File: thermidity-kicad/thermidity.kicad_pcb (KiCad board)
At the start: 2 copper layers, 21 parts, among them J1 Battery, J2 Display, J3 ISP, U1 ATmega328P-A, U2 MCP1501-30xSN, U3 TMP36GT9, U4 HIH-5030-001, Y1 32.768kHz Watch Crystal 10pF 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

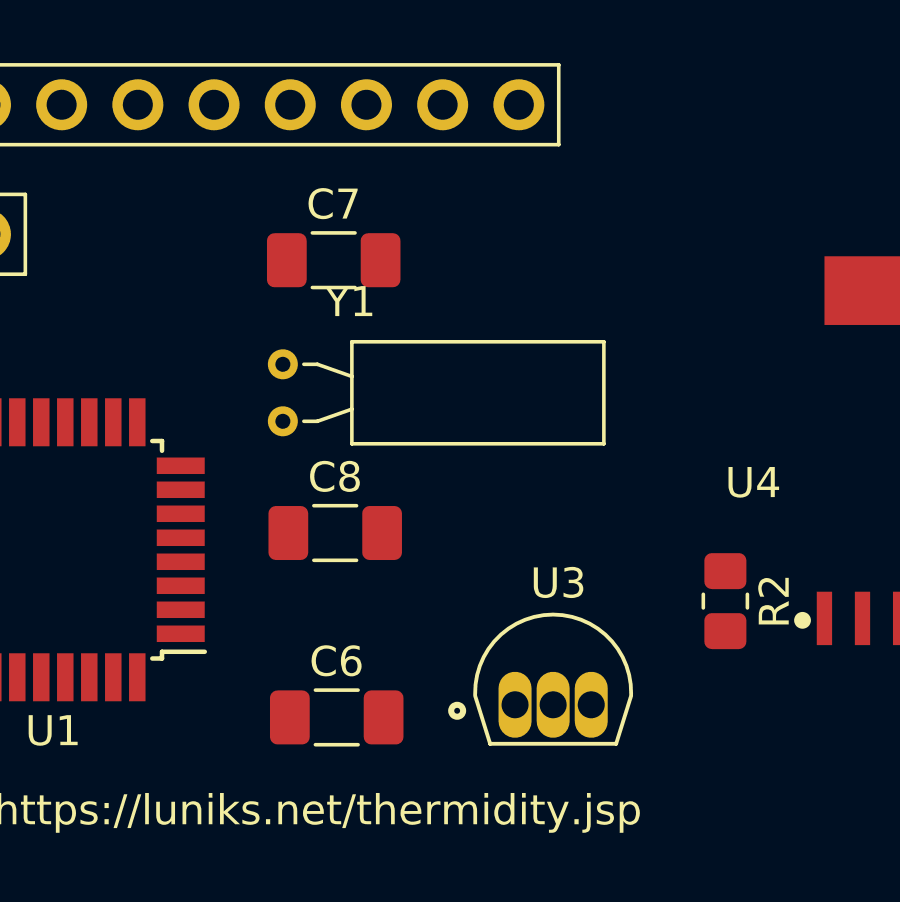
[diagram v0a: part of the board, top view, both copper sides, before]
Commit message: update README, schematic + PCB (remove crystal)
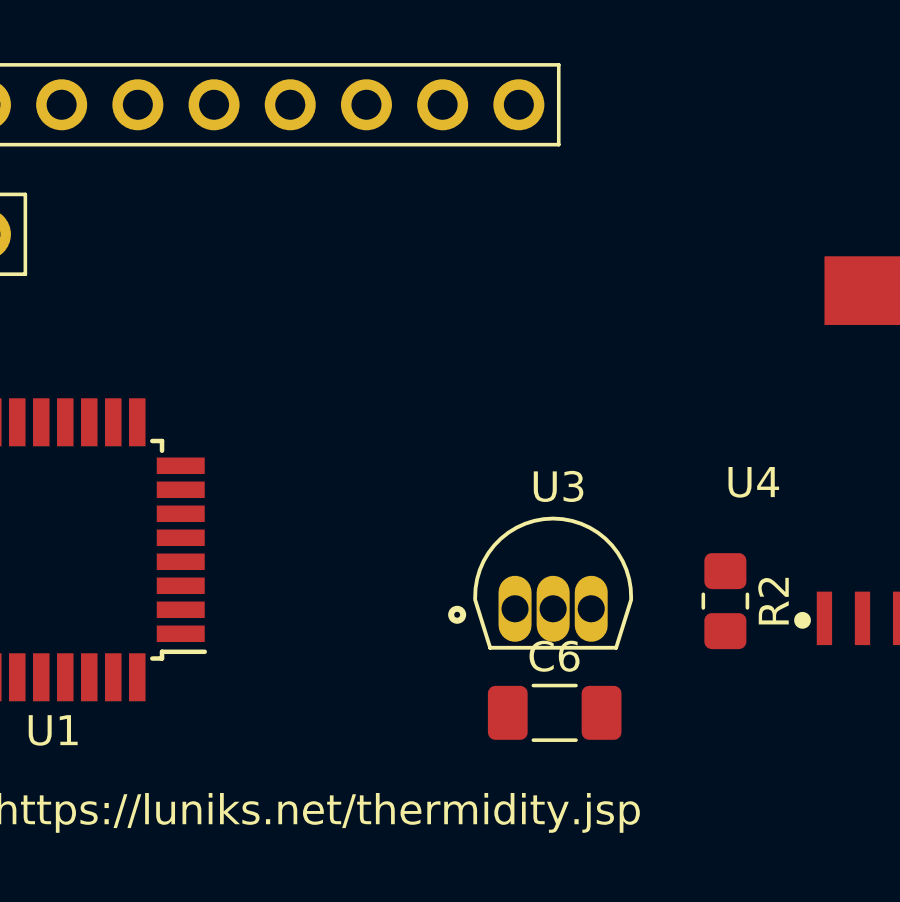
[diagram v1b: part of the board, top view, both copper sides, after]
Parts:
- removed C7, C8: 18pF, Capacitor_SMD:C_1206_3216Metric_Pad1.33x1.80mm_HandSolder
- removed Y1: 32.768kHz Watch Crystal 10pF 35kOhm, Crystal:Crystal_C38-LF_D3.0mm_L8.0mm_Horizontal
- moved C6 7.27 mm to (158.1, 81.0)
- moved U3 3.20 mm to (158.1, 76.7)
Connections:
- U1 pad 7: Net-(C8-Pad1) -> unconnected-(U1-Pad7)
- U1 pad 8: Net-(C7-Pad1) -> unconnected-(U1-Pad8)

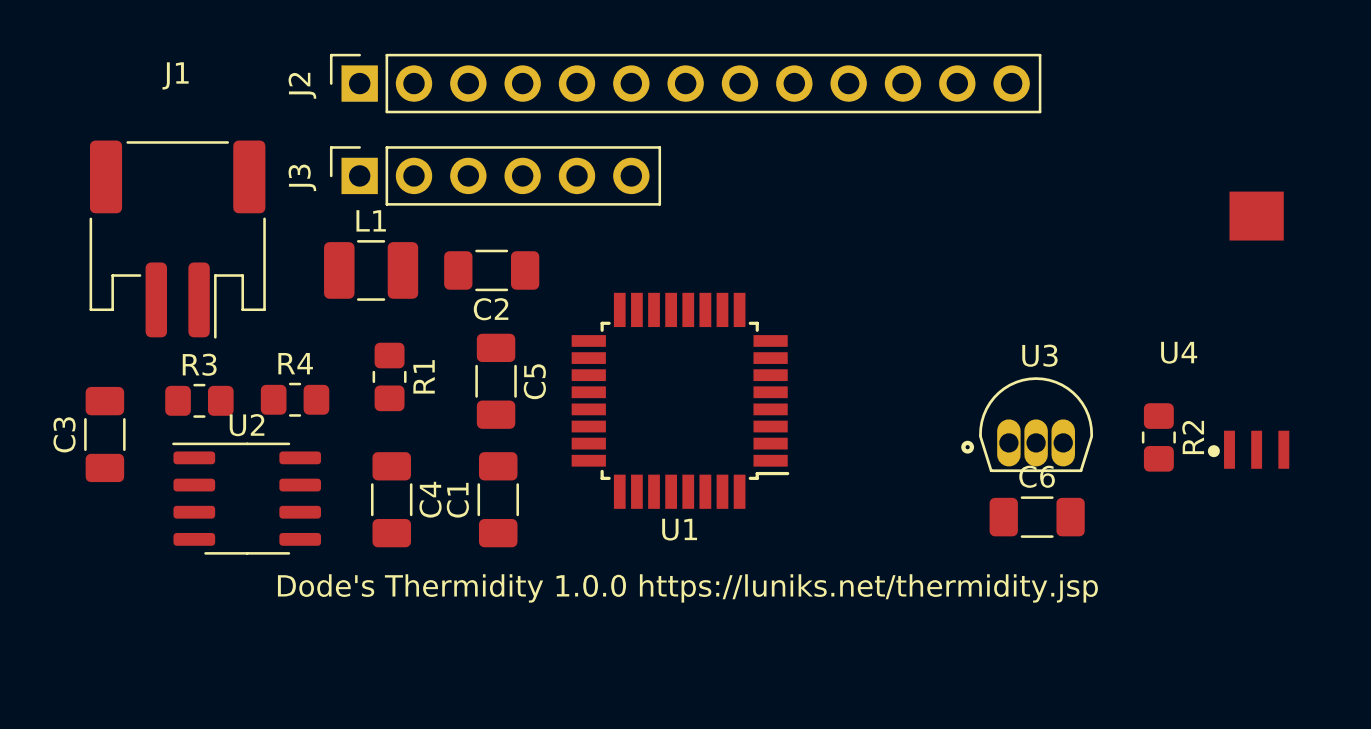
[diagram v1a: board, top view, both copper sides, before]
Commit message: improve PCB, add comments
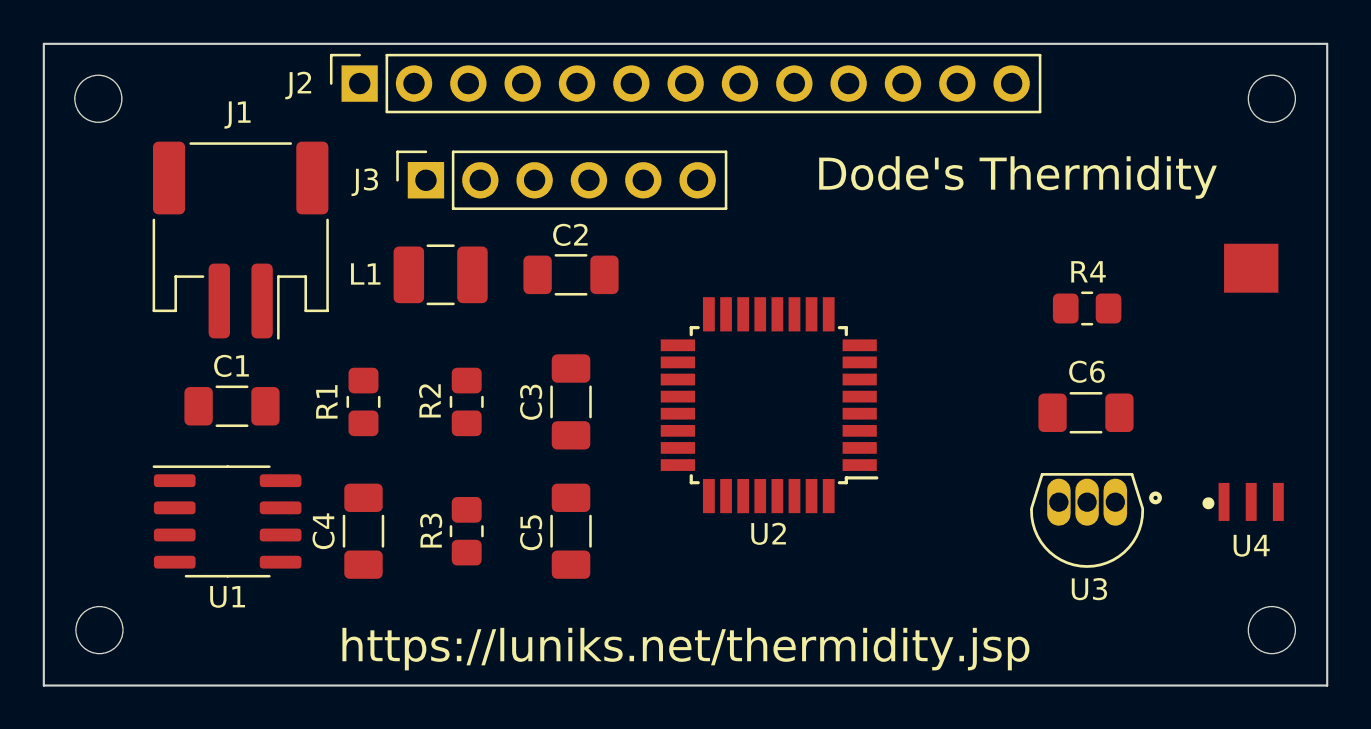
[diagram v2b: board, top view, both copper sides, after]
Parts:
- added H1: M2, MountingHole:MountingHole_2.2mm_M2, F.Cu at (114.2, 61.5)
- added H2: M2, MountingHole:MountingHole_2.2mm_M2, F.Cu at (169.1, 61.5)
- added H3: M2, MountingHole:MountingHole_2.2mm_M2, F.Cu at (114.3, 86.3)
- added H4: M2, MountingHole:MountingHole_2.2mm_M2, F.Cu at (169.1, 86.3)
- U1: renamed from U2; value MCP1501-30xSN -> MCP1501-30
- U2: renamed from U1; value ATmega328P-A -> ATmega328P
- U3: value TMP36GT9 -> TMP36
- U4: value HIH-5030-001 -> HIH-5030
- moved R2 12.5 mm to (131.5, 75.6), turned to -90 degrees
- moved R3 10.1 mm to (131.5, 81.7), turned to -90 degrees
- moved R4 6.90 mm to (160.5, 71.3), turned to 180 degrees
- moved C1 6.09 mm to (120.5, 75.8), turned to 0 degrees
- moved C6 5.39 mm to (160.4, 76.1), turned to 180 degrees
- moved U3 5.16 mm to (160.5, 81.2), turned to 180 degrees
- moved U2 4.17 mm to (145.6, 75.8)
- moved C2 3.71 mm to (136.3, 69.7), turned to 0 degrees
- moved C5 3.71 mm to (136.3, 81.7)
- moved C3 3.64 mm to (136.3, 75.6), turned to 90 degrees
- moved L1 3.26 mm to (130.3, 69.7)
- moved J3 3.11 mm to (129.6, 65.3)
- moved J1 2.95 mm to (120.9, 68.1)
- moved U4 2.45 mm to (168.1, 75.0)
- moved C4 1.98 mm to (126.6, 81.7)
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- renumbered C3 to C1, C5 to C3, C1 to C5, R3 to R2, R4 to R3, R2 to R4
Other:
- board outline added: 60 x 30 mm
- board text added: "Dode's Thermidity"
- board text added: "https://luniks.net/thermidity.jsp"
- board text removed: "Dode's Thermidity 1.0.0 https://luniks.net/thermidity.jsp"

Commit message: improve PCB, add comments
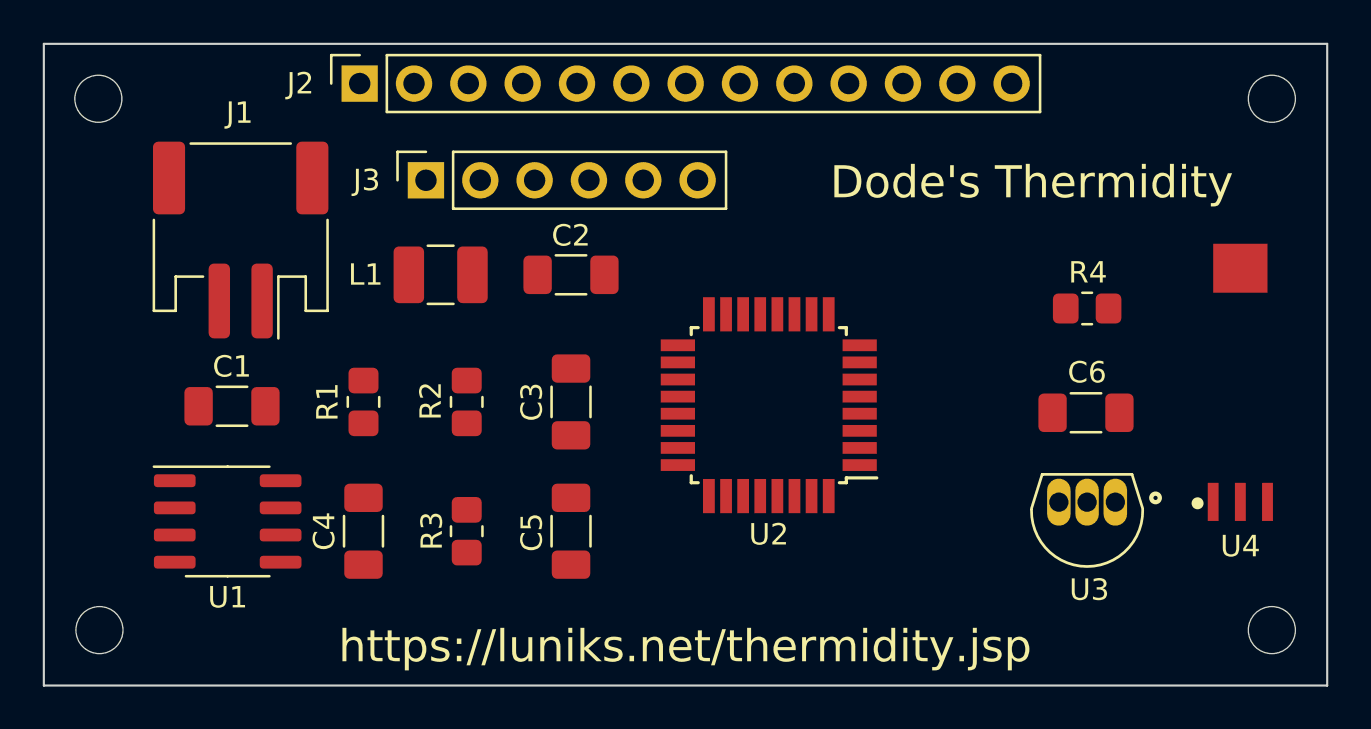
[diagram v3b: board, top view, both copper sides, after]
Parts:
- R1: value 50Ohm -> 50
- moved U4 0.51 mm to (167.6, 75.0)
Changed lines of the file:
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@@
   )
   (footprint "HIH-5030-001:HONEYWELL_HIH-5030-001" (layer "F.Cu")
-    (at 168.148 74.9808)
+    (at 167.64 74.9808)
     (property "AVAILABILITY" "Good")
     (property "MF" "Honeywell")
@@
       (effects (font (size 1 1) (thickness 0.15)))
     )
-    (fp_text value "50Ohm" (at 0 -1.778 90) (layer "F.Fab")
+    (fp_text value "50" (at 0 -1.778 90) (layer "F.Fab")
       (effects (font (size 1 1) (thickness 0.15)))
     )
@@
   (gr_rect (start 111.7 58.9) (end 171.7 88.9) (layer "Edge.Cuts") (width 0.1) (fill none))
   (gr_rect (start 111.7 58.9) (end 171.7 88.9) (layer "F.CrtYd") (width 0.05) (fill none))
-  (gr_text "Dode's Thermidity" (at 157.1752 65.024) (layer "F.SilkS")
+  (gr_text "Dode's Thermidity" (at 157.8864 65.3796) (layer "F.SilkS")
     (effects (font (size 1.5 1.5) (thickness 0.15)))
   )

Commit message: improve PCB
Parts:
- moved C5 25.9 mm to (136.0, 84.8), turned to -90 degrees
- moved U3 19.5 mm to (141.3, 84.8), turned to -90 degrees
- moved C6 18.8 mm to (153.4, 73.9)
- moved R4 18.2 mm to (148.3, 84.8)
- moved U4 13.5 mm to (158.4, 84.8), turned to -90 degrees
- moved C1 9.95 mm to (130.2, 73.7), turned to 180 degrees
- moved R2 7.02 mm to (137.0, 77.4), turned to 180 degrees
- moved R3 6.96 mm to (137.0, 79.9), turned to 0 degrees
- moved C4 5.95 mm to (131.7, 84.8)
- moved R1 5.73 mm to (131.7, 78.3)
- moved U1 5.58 mm to (125.5, 79.1)
- moved C3 1.98 mm to (136.4, 73.7), turned to 0 degrees
- moved U2 1.84 mm to (145.4, 74.0)
- moved J3 0.51 mm to (129.1, 65.3)
- renumbered C6 to C5, C5 to C6, R3 to R2, R2 to R3
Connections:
- R2 pad 1: Net-(R3-Pad2) -> Net-(U2-Pad24)
- R3 pad 2: Net-(R3-Pad2) -> Net-(U2-Pad24)
- R4 pad 1: Net-(R2-Pad1) -> Net-(U2-Pad26)
- U2 pad 23: Net-(U1-Pad23) -> unconnected-(U2-Pad23)
- U2 pad 24: Net-(R2-Pad1) -> Net-(U2-Pad24)
- U2 pad 25: Net-(R3-Pad2) -> Net-(U2-Pad25)
- U2 pad 26: unconnected-(U1-Pad26) -> Net-(U2-Pad26)
- U3 pad 2: Net-(U1-Pad23) -> Net-(U2-Pad25)
- U4 pad 2: Net-(R2-Pad1) -> Net-(U2-Pad26)
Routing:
- net +BATT: track 0.00 -> 81.8 mm, vias 0 -> 4
- net Net-(C3-Pad2): track 0.00 -> 49.8 mm
- net GND: track 0.00 -> 33.9 mm, vias 0 -> 12
- net Net-(J3-Pad2): track 0.00 -> 22.2 mm, vias 0 -> 2
- net Net-(J2-Pad4): track 0.00 -> 13.4 mm
- net Net-(U2-Pad26): track 0.00 -> 12.9 mm
- net Net-(J2-Pad12): track 0.00 -> 11.5 mm
- net Net-(J2-Pad5): track 0.00 -> 11.4 mm
- net Net-(C2-Pad2): track 0.00 -> 11.4 mm
- net Net-(J2-Pad11): track 0.00 -> 10.8 mm
- net Net-(J2-Pad6): track 0.00 -> 10.7 mm
- net Net-(J2-Pad7): track 0.00 -> 10.3 mm
- net Net-(J2-Pad8): track 0.00 -> 9.62 mm
- net Net-(J2-Pad9): track 0.00 -> 9.02 mm
- net Net-(U2-Pad25): track 0.00 -> 7.83 mm
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- added copper zone on B.Cu, net GND
- added copper zone on F.Cu, net GND
